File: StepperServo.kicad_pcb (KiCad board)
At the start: 4 copper layers, 35.5 x 35.5 mm, 77 parts, among them J1 Conn_01x01_Female, J2 Conn_01x01_Female, J3 Conn_01x04_Male, J4 I2C_External, J6 Conn_TempMotor, SW4 SW_Reset, U1 TC1185, U2 SN65HVD232, U3 TMC2209-LA, U5 STM32F103RETx, U6 AS5600, U7 INA180A1, Y1 ABM3B-16MHz

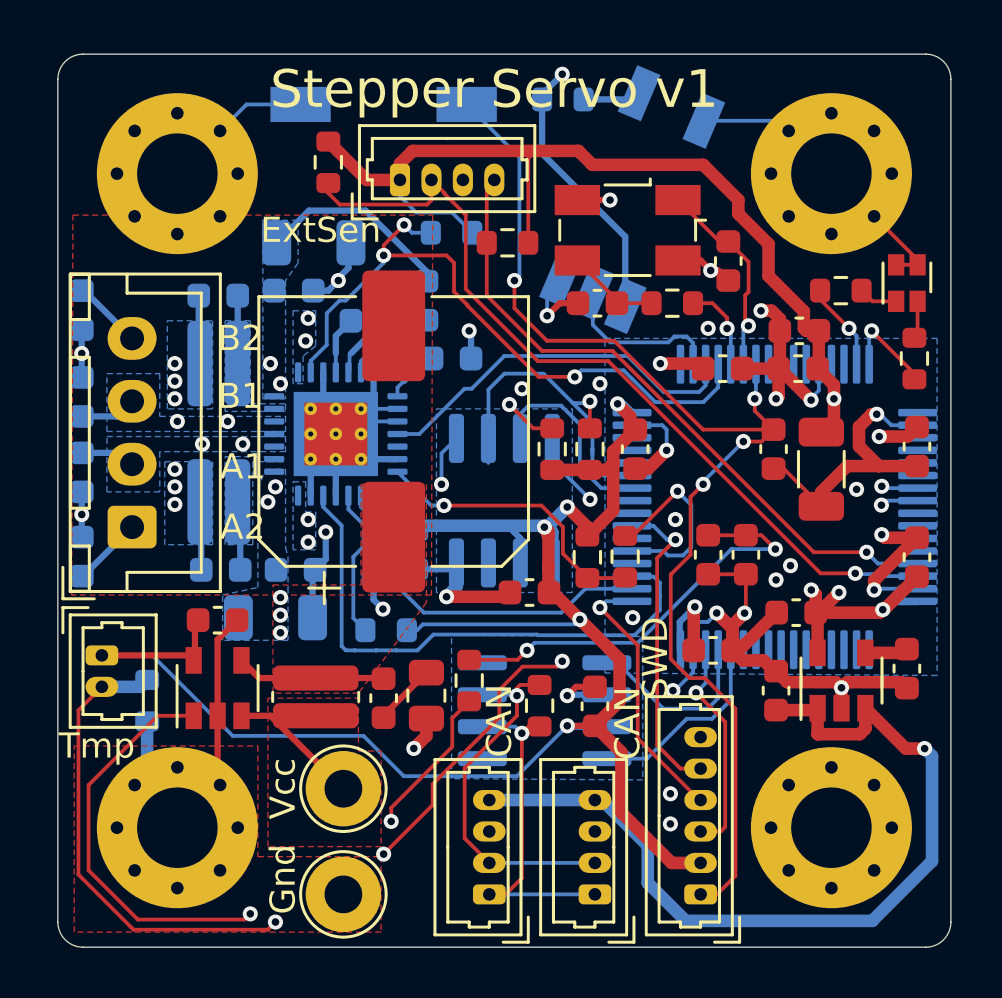
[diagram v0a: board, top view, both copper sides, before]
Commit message: Update to KiCad 6.0.0
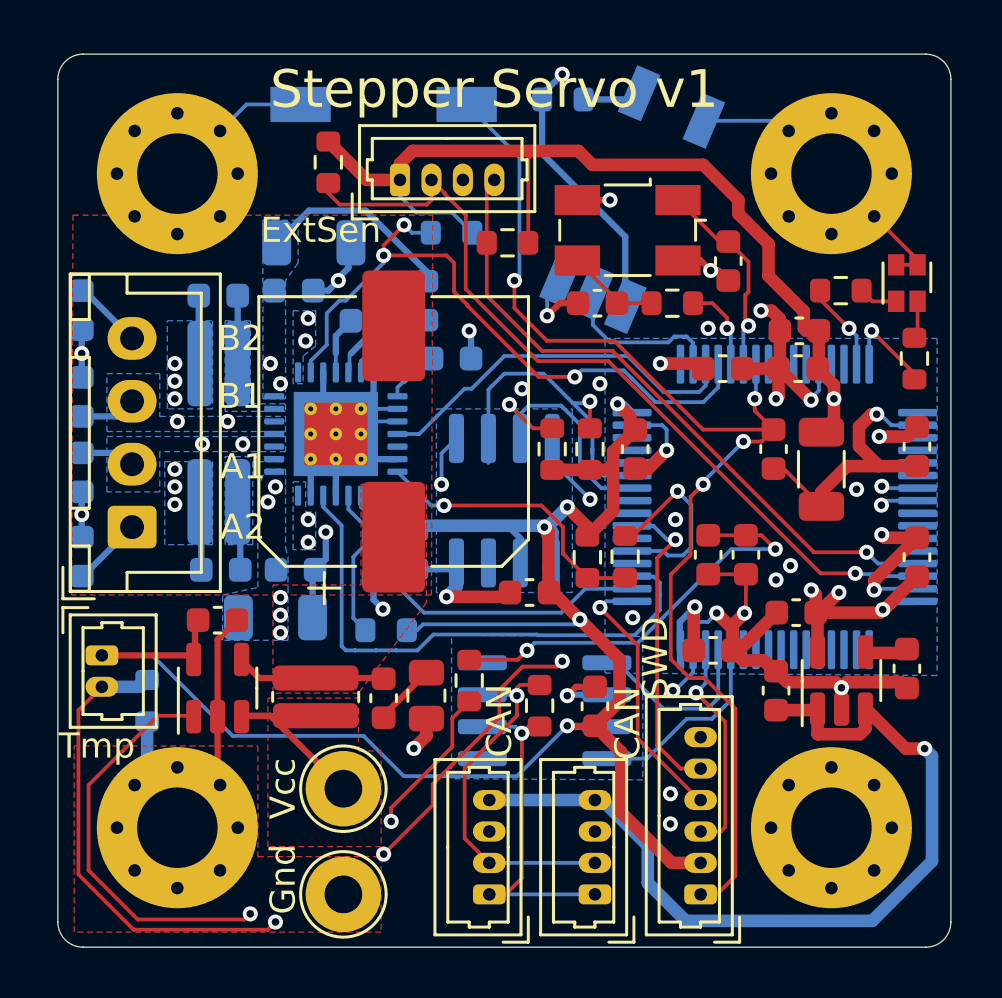
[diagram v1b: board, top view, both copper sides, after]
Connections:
- net /MCU/~RST renamed /MCU/~{RST}
- net /StepperDriver/~EN renamed /StepperDriver/~{EN}
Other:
- net class Default removed
- net class smol removed
